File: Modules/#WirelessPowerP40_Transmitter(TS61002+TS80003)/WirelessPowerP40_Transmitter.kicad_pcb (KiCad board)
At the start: 4 copper layers, 53 x 53 mm, 133 parts, among them J1 USBA, J2 I2C, J3 I2C, J4 Coil Therm, J5 COIL 20uH, J6 Conn_01x02_Male, J7 Conn_01x02_Male, U1 TS30041, U2 TS94033, U3 74LVC1G66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

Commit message: WirelessPowerP40_Transmitter optimization
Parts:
- L2: value 600 -> 1uF
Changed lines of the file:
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@@
       (effects (font (size 0.6 0.6) (thickness 0.1)))
     )
-    (fp_text value "600" (at 0 3 -270) (layer "F.Fab")
+    (fp_text value "1uF" (at 0 3 -270) (layer "F.Fab")
       (effects (font (size 1 1) (thickness 0.15)))
     )
@@
   (segment (start 151.83 84.2) (end 151.83 79.73) (width 0.3) (layer "In1.Cu") (net 55))
   (segment (start 151.83 79.73) (end 152.2 79.36) (width 0.3) (layer "In1.Cu") (net 55))
-  (segment (start 152.2 80.43) (end 152.2 79.36) (width 0.25) (layer "In2.Cu") (net 55))
-  (segment (start 148.99 83.64) (end 152.2 80.43) (width 0.25) (layer "In2.Cu") (net 55))
   (segment (start 129.33 82.94) (end 129.33 82.96) (width 0.25) (layer "In2.Cu") (net 55))
+  (segment (start 152.2 80.59) (end 152.2 79.36) (width 0.25) (layer "In2.Cu") (net 55))
+  (segment (start 149.15 83.64) (end 152.2 80.59) (width 0.25) (layer "In2.Cu") (net 55))
   (segment (start 129.33 82.96) (end 130.01 83.64) (width 0.25) (layer "In2.Cu") (net 55))
-  (segment (start 130.01 83.64) (end 148.99 83.64) (width 0.25) (layer "In2.Cu") (net 55))
+  (segment (start 130.01 83.64) (end 149.15 83.64) (width 0.25) (layer "In2.Cu") (net 55))
   (segment (start 149.079999 74.470001) (end 149.25 74.3) (width 0.25) (layer "F.Cu") (net 56))
   (segment (start 158.77 96) (end 158.21 96.56) (width 0.25) (layer "F.Cu") (net 56))

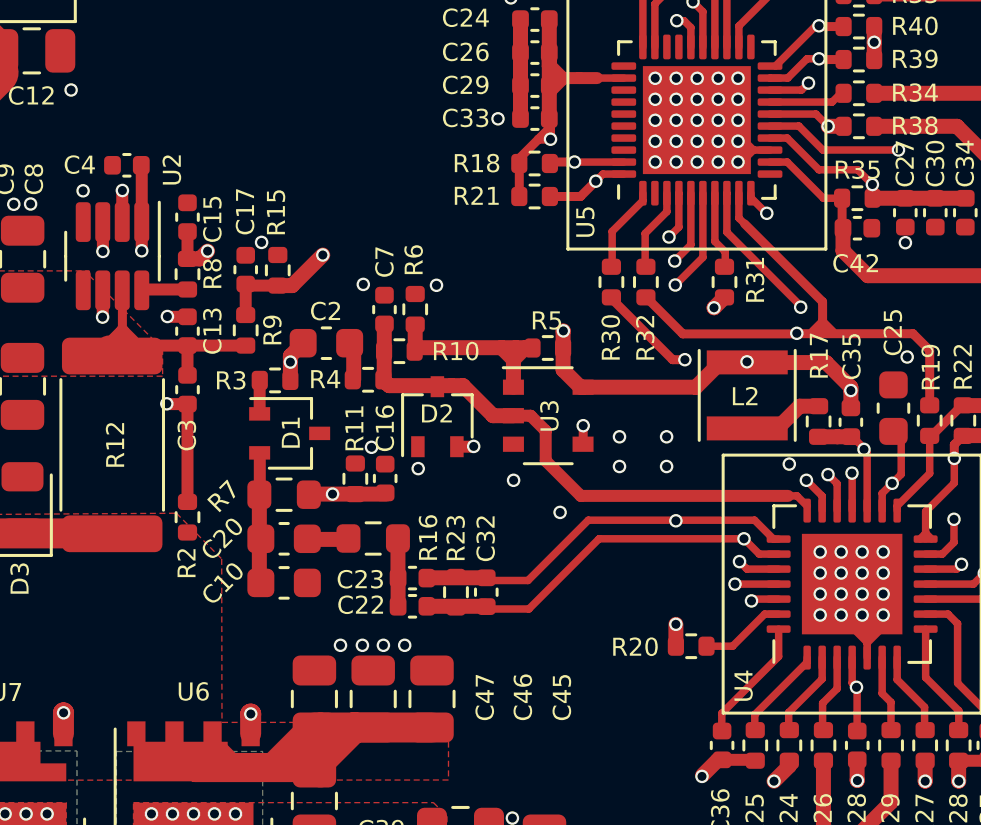
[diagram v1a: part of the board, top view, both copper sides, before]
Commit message: replace low Vr diode BAT54 with BAS101s in WirelessPowerP40_Transmitter
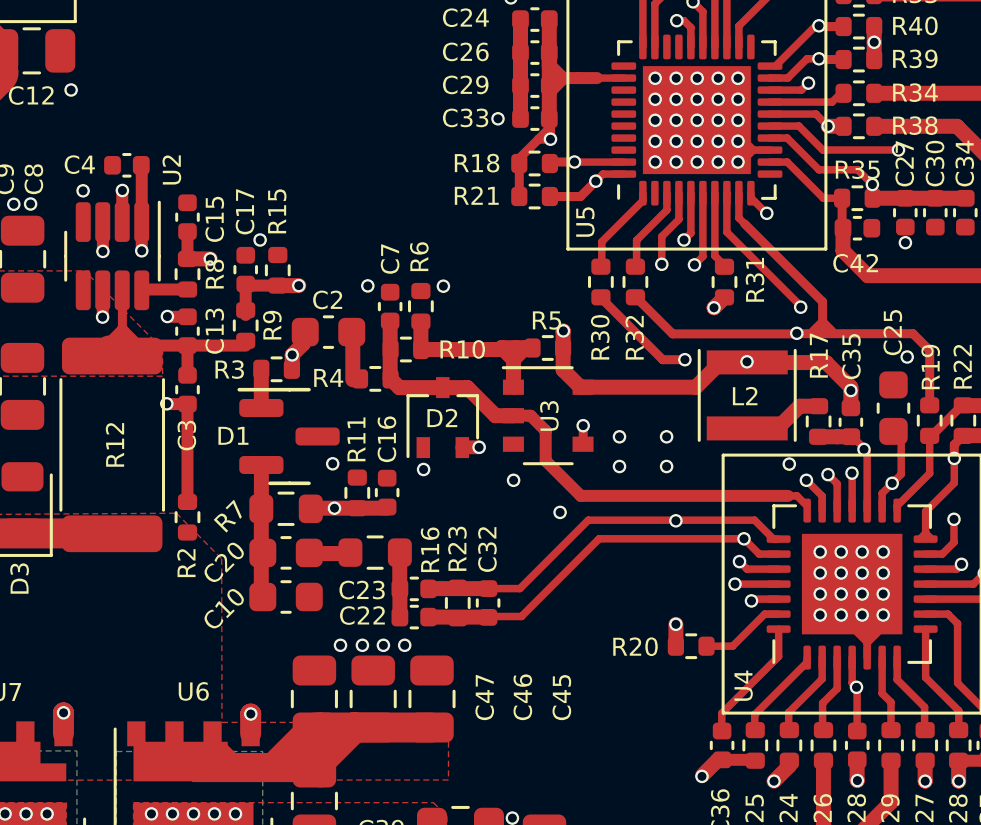
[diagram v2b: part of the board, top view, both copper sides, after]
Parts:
- D1: value BAT54SW -> BAS101S,215; footprint Package_TO_SOT_SMD:SOT-323_SC-70 -> Package_TO_SOT_SMD:SOT-23
- moved C10 0.47 mm to (134.8, 96.5)
- moved C16 0.47 mm to (138.2, 93.0)
- moved C20 0.47 mm to (134.8, 95.0)
- moved R11 0.47 mm to (137.2, 93.0)
- moved R16 0.47 mm to (137.8, 95.0)
- moved R7 0.47 mm to (134.8, 93.5)
- moved C2 0.38 mm to (136.2, 87.7)
- moved R3 0.37 mm to (134.5, 88.9)
- moved C22 0.36 mm to (139.1, 97.2)
- moved C23 0.36 mm to (139.1, 96.2)
- moved C32 0.36 mm to (141.5, 96.7)
- moved R23 0.36 mm to (140.5, 96.7)
- moved R32 0.35 mm to (146.4, 86.0)
- moved R30 0.35 mm to (145.3, 86.0)
- moved R4 0.24 mm to (137.8, 89.2)
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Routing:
- net DC_FBI: track 20.4 -> 19.4 mm

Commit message: add PD(19V3A) support for WirelessPowerP40_Transmitter
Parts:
- added U10: HUSB238, Package_DFN_QFN:DFN-10-1EP_3x3mm_P0.5mm_EP1.65x2.38mm, F.Cu at (113.0, 101.1)
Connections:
- J1 pad 2: unconnected-(J1-Pad2) -> D-
- J1 pad 3: unconnected-(J1-Pad3) -> D+
- J1 pad 5: unconnected-(J1-Pad5) -> CC
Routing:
- net D-: track 0.00 -> 15.9 mm, vias 0 -> 1
- net CC: track 0.00 -> 13.8 mm, vias 0 -> 1
- net D+: track 0.00 -> 11.0 mm, vias 0 -> 1
- net DC_I-: track 25.8 -> 29.6 mm

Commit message: WirelessPowerP40_Transmitter > change D3 value with pacific diode
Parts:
- D3: value 28V -> BZT52C30 30V
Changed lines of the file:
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@@
       (effects (font (size 0.6 0.6) (thickness 0.1)))
     )
-    (fp_text value "28V" (at 0 1.65 90) (layer "F.Fab")
+    (fp_text value "BZT52C30 30V" (at 0 1.65 90) (layer "F.Fab")
       (effects (font (size 1 1) (thickness 0.15)))
     )

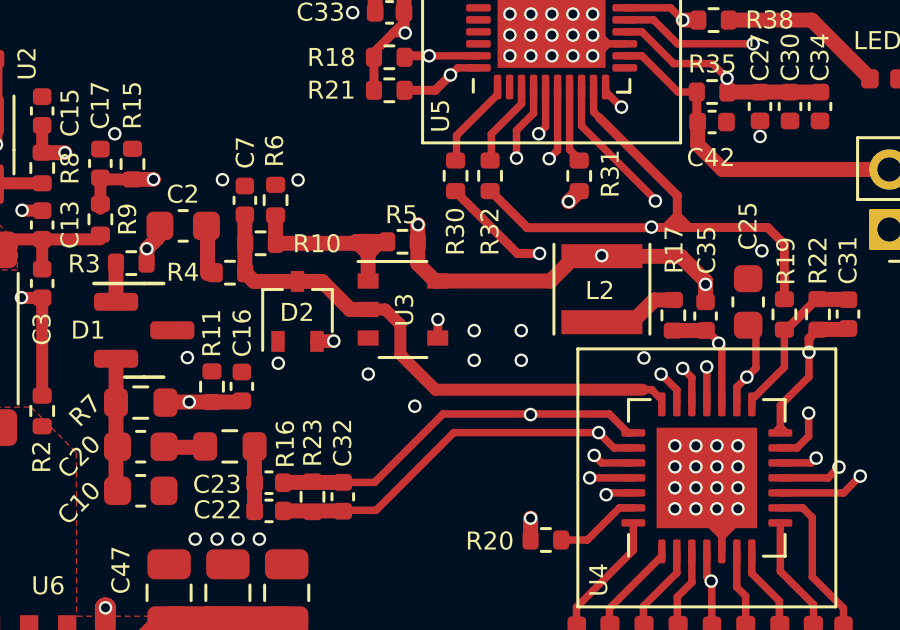
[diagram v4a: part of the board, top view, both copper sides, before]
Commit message: fix footprint of 74lvc
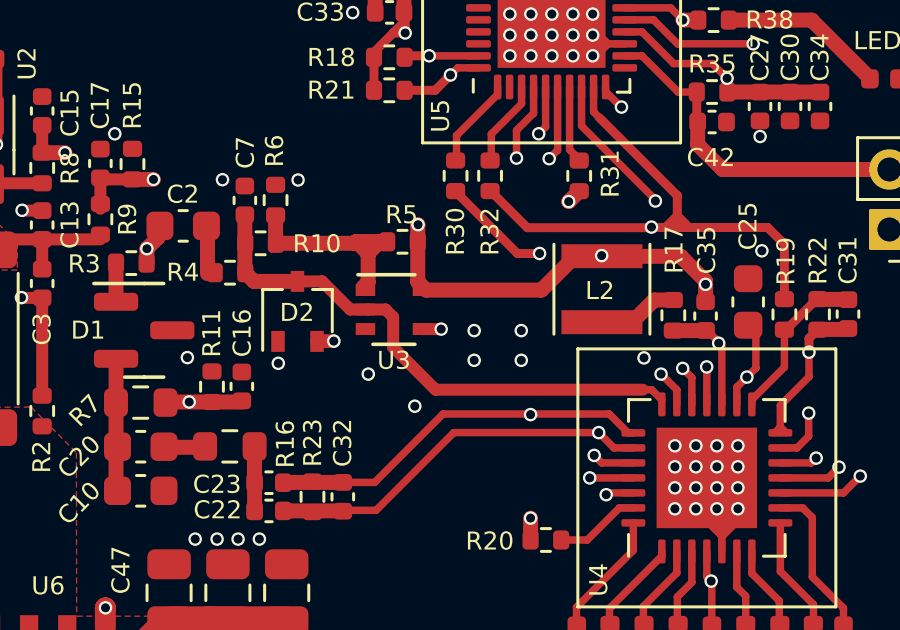
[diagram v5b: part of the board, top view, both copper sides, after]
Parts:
- C55: value 4.7uF -> 4.7uF 25V
- U3: footprint Package_SO:TSOP-5_1.65x3.05mm_P0.95mm -> Package_TO_SOT_SMD:SOT-353_SC-70-5
- moved U3 0.30 mm to (143.2, 90.4)
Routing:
- net VDDA: track 53.4 -> 54.0 mm

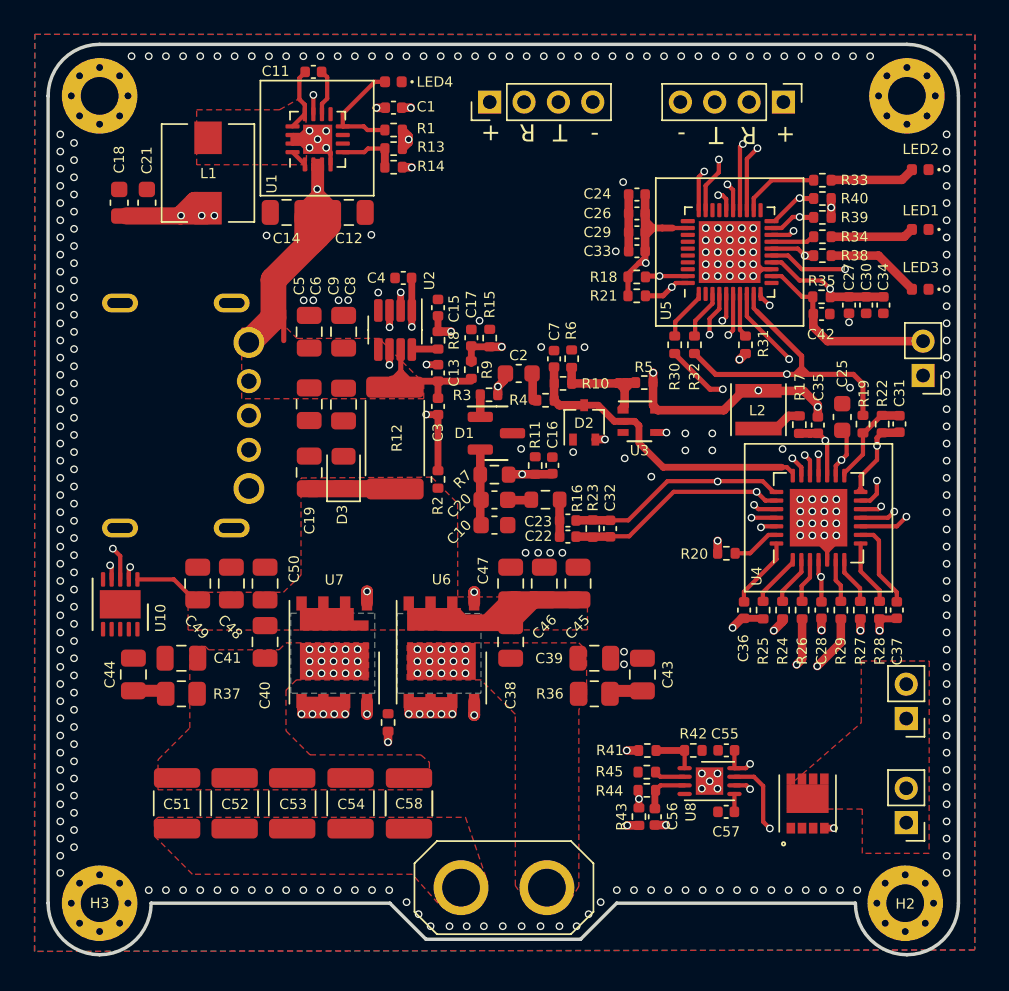
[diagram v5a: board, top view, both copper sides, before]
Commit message: replace USB Connector
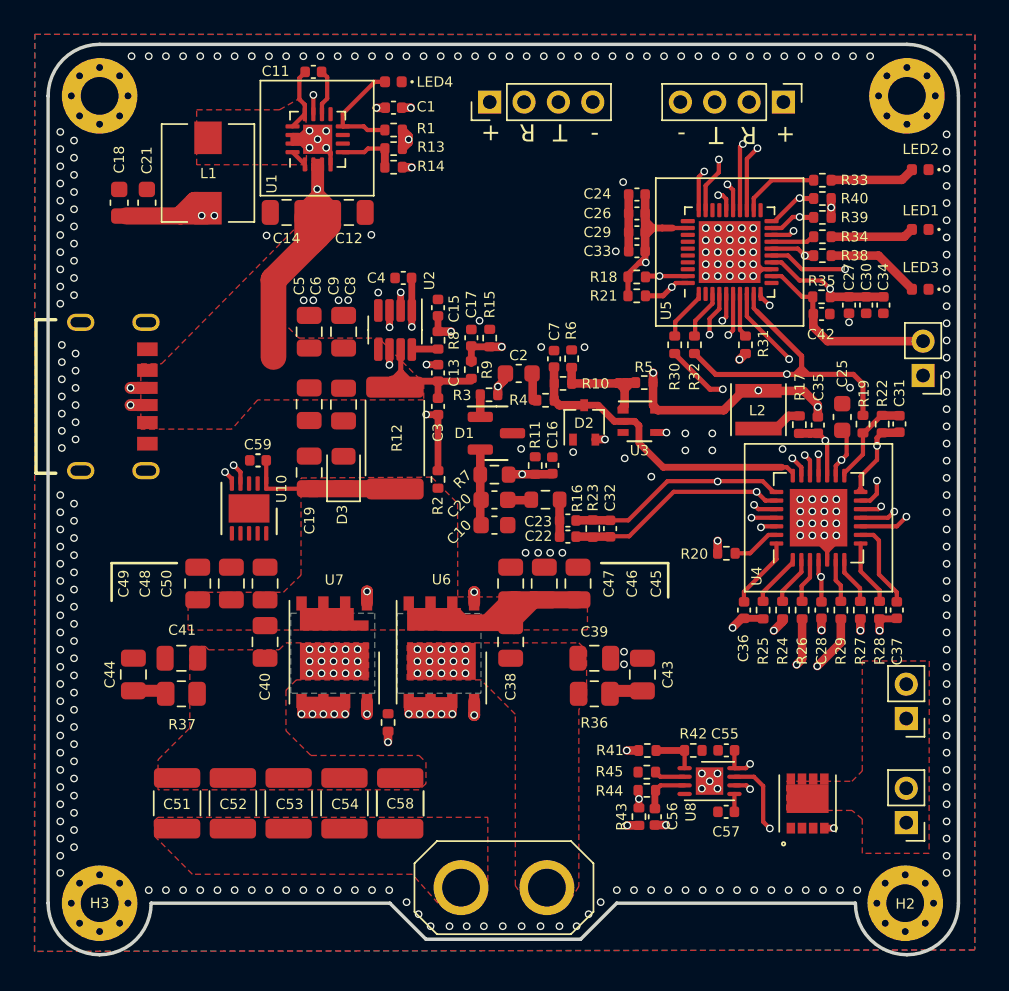
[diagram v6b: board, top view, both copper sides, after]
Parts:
- added C59: 1uF 50V, Capacitor_SMD:C_0402_1005Metric, F.Cu at (121.0, 92.7)
- J1: footprint USB_plug:USB_A_2.0_FAST -> USB_plug:USB4125-GF-A_REVA2
- moved U10 9.35 mm to (120.5, 95.5)
- moved J1 8.07 mm to (111.5, 89.0), turned to -90 degrees
- moved C58 0.51 mm to (129.3, 112.7)
- moved C54 0.36 mm to (126.1, 112.7)
- moved C53 0.21 mm to (122.8, 112.7)
- moved C52 0.10 mm to (119.6, 112.7)
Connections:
- U10 pad 2: D+ -> unconnected-(U10-Pad2)
- U10 pad 3: D- -> unconnected-(U10-Pad3)
- U10 pad 4: CC -> CC1
- U10 pad 5: unconnected-(U10-Pad5) -> CC2
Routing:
- net D-: track 15.9 -> 0.00 mm, vias 1 -> 0
- net CC: track 13.8 -> 0.00 mm, vias 1 -> 0
- net D+: track 11.0 -> 0.00 mm, vias 1 -> 0
- net CC1: track 0.00 -> 10.1 mm, vias 0 -> 2
- net CC2: track 0.00 -> 8.95 mm, vias 0 -> 2
- net DC_I+: track 57.3 -> 55.8 mm
- net +5V: track 117.9 -> 116.8 mm, vias 11 -> 10
- net GND: track 35.4 -> 35.2 mm, vias 310 -> 302

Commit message: update USB-Type-C,with QC support
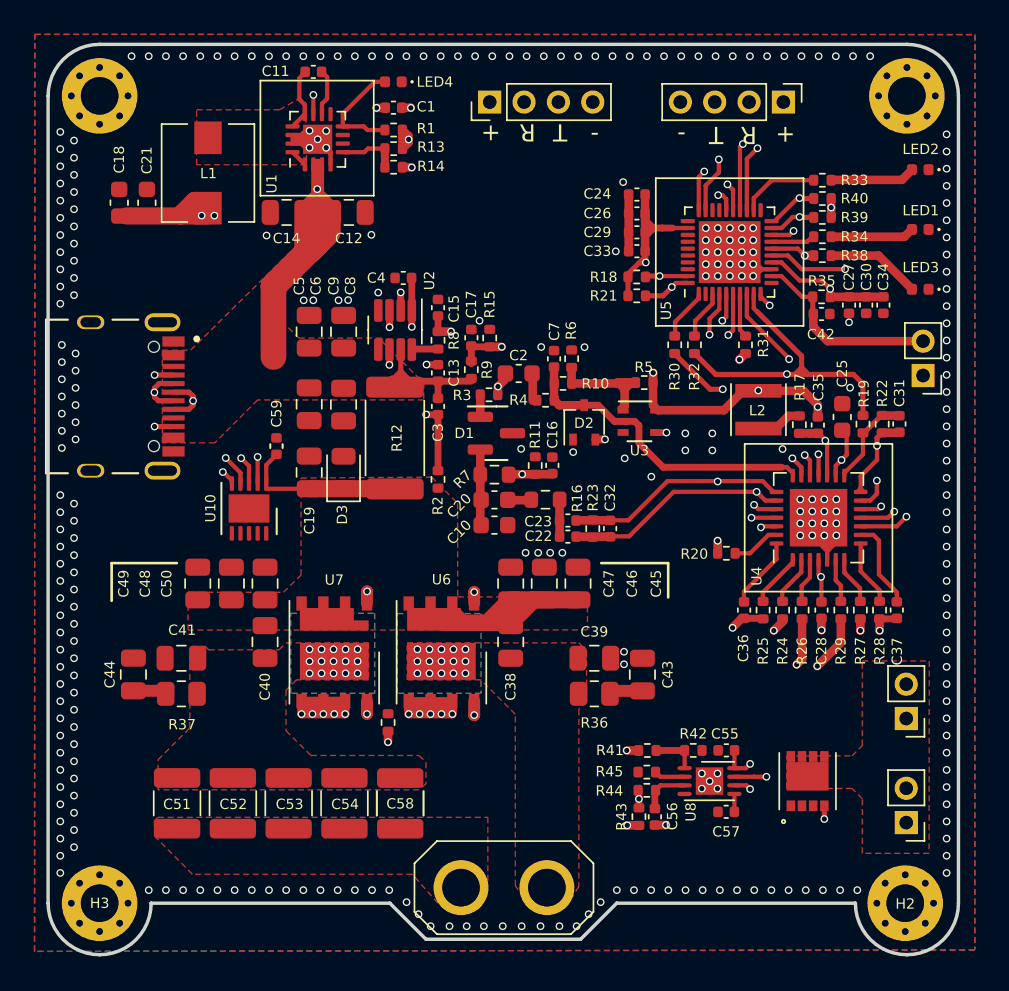
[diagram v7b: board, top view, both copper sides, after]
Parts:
- J1: footprint USB_plug:USB4125-GF-A_REVA2 -> USB_plug:SHENZHEN-CHUANGQIN-TECHNOLOGY_CQ-USB-C16PSMT01
- moved J1 4.60 mm to (116.1, 89.0)
- moved C59 1.36 mm to (122.1, 91.9), turned to -90 degrees
- moved U9 1.30 mm to (153.0, 111.4)
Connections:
- U10 pad 2: unconnected-(U10-Pad2) -> D+
- U10 pad 3: unconnected-(U10-Pad3) -> D-
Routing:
- net D-: track 0.00 -> 11.2 mm, vias 0 -> 2
- net D+: track 0.00 -> 9.66 mm, vias 0 -> 2
- net CC2: track 8.95 -> 7.08 mm
- net Net-(U8-Pad7): track 8.82 -> 7.02 mm
- net DC_I+: track 55.8 -> 57.2 mm
- net CC1: track 10.1 -> 10.9 mm
- net DC_I-: track 29.7 -> 30.3 mm

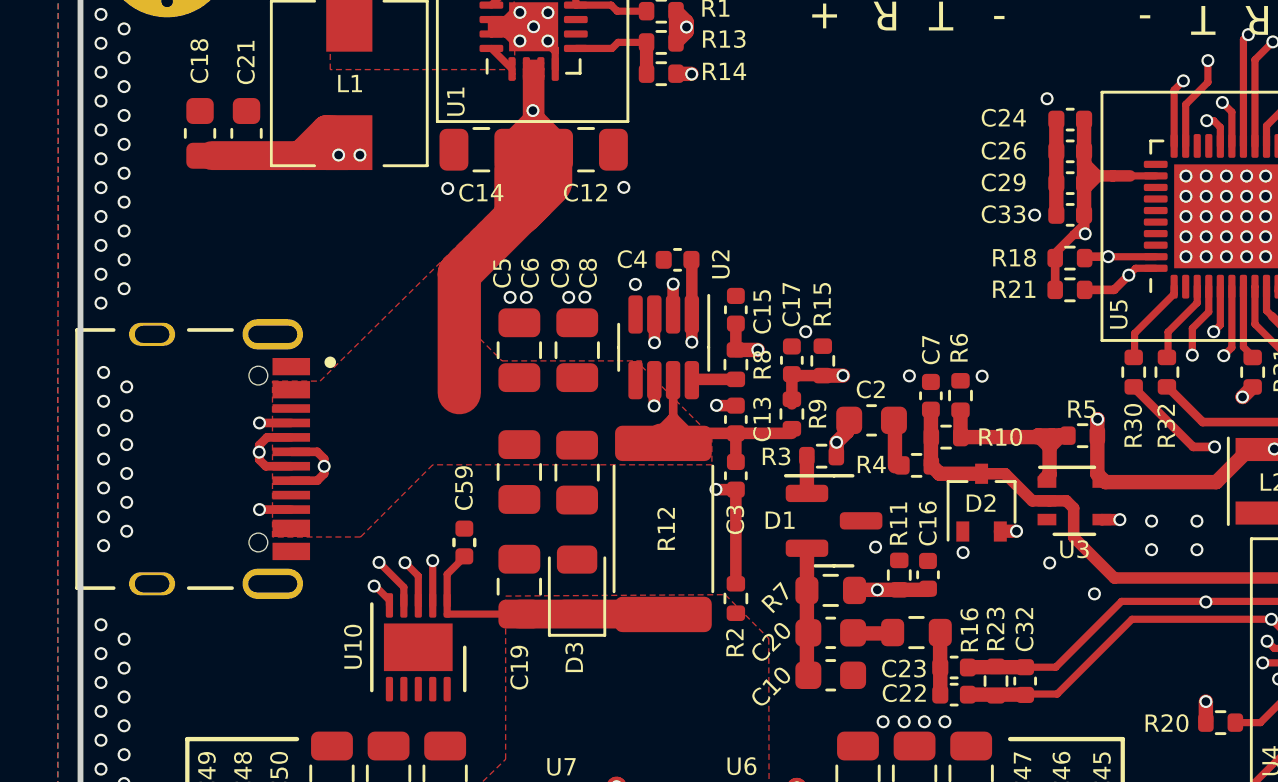
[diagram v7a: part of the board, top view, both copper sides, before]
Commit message: rollback (PD3.0 fix)
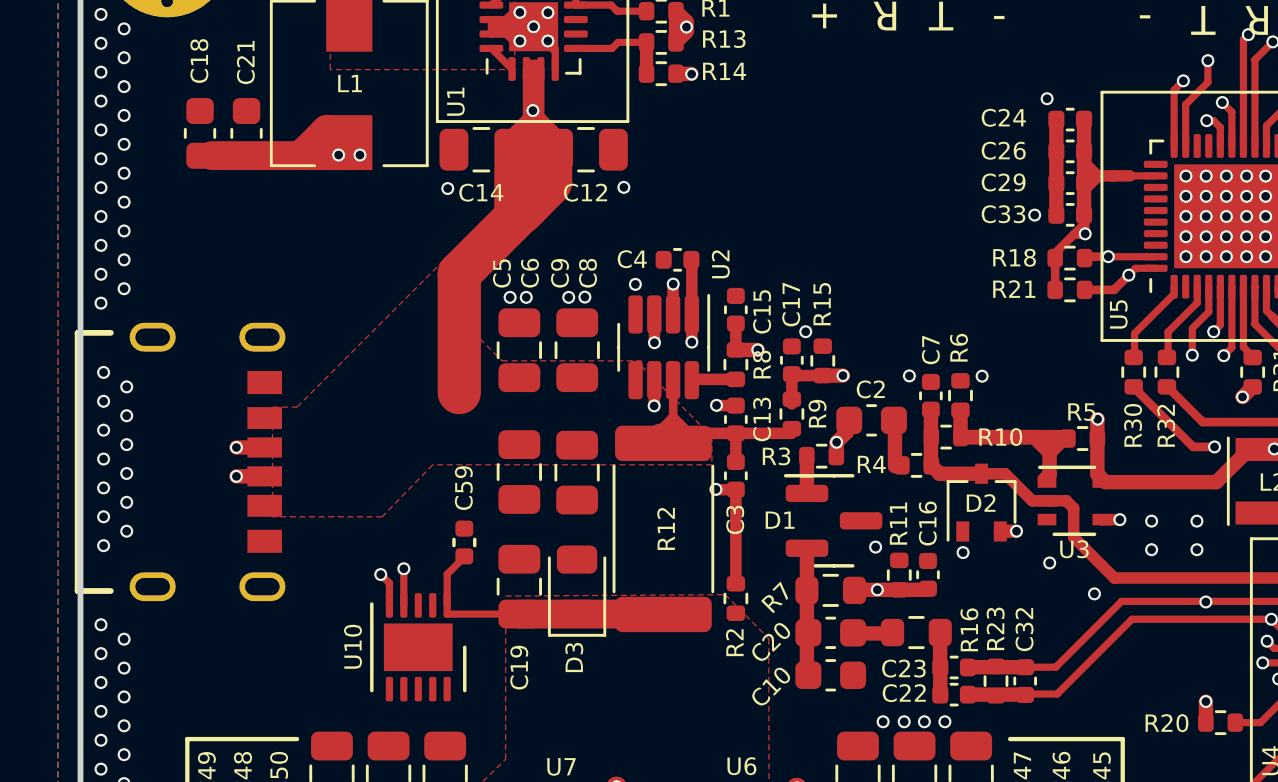
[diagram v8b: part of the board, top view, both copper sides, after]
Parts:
- J1: footprint USB_plug:SHENZHEN-CHUANGQIN-TECHNOLOGY_CQ-USB-C16PSMT01 -> USB_plug:USB4125-GF-A_REVA2
- moved J1 4.00 mm to (112.1, 89.1)
- moved R5 0.10 mm to (143.5, 88.3)
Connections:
- U10 pad 2: D+ -> unconnected-(U10-Pad2)
- U10 pad 3: D- -> unconnected-(U10-Pad3)
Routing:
- net D-: track 11.2 -> 0.00 mm, vias 2 -> 0
- net D+: track 9.66 -> 0.00 mm, vias 2 -> 0
- net Net-(R10-Pad1): track 7.30 -> 9.91 mm
- net CC2: track 7.08 -> 8.58 mm
- net +5V: track 117.2 -> 115.9 mm
- net CC1: track 10.9 -> 9.79 mm
